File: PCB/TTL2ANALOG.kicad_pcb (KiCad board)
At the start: 2 copper layers, 60.5 x 56.1 mm, 35 parts, among them J1 EGA/CGA, J2 Brown Fix, J3 CSync Inv., J4 Sync Type, J5 TTL Input, J6 Analog Out, J7 Barrel_Jack, U1 GAL16V8, U2 74LS244, U3 74LS244, U4 L78L05

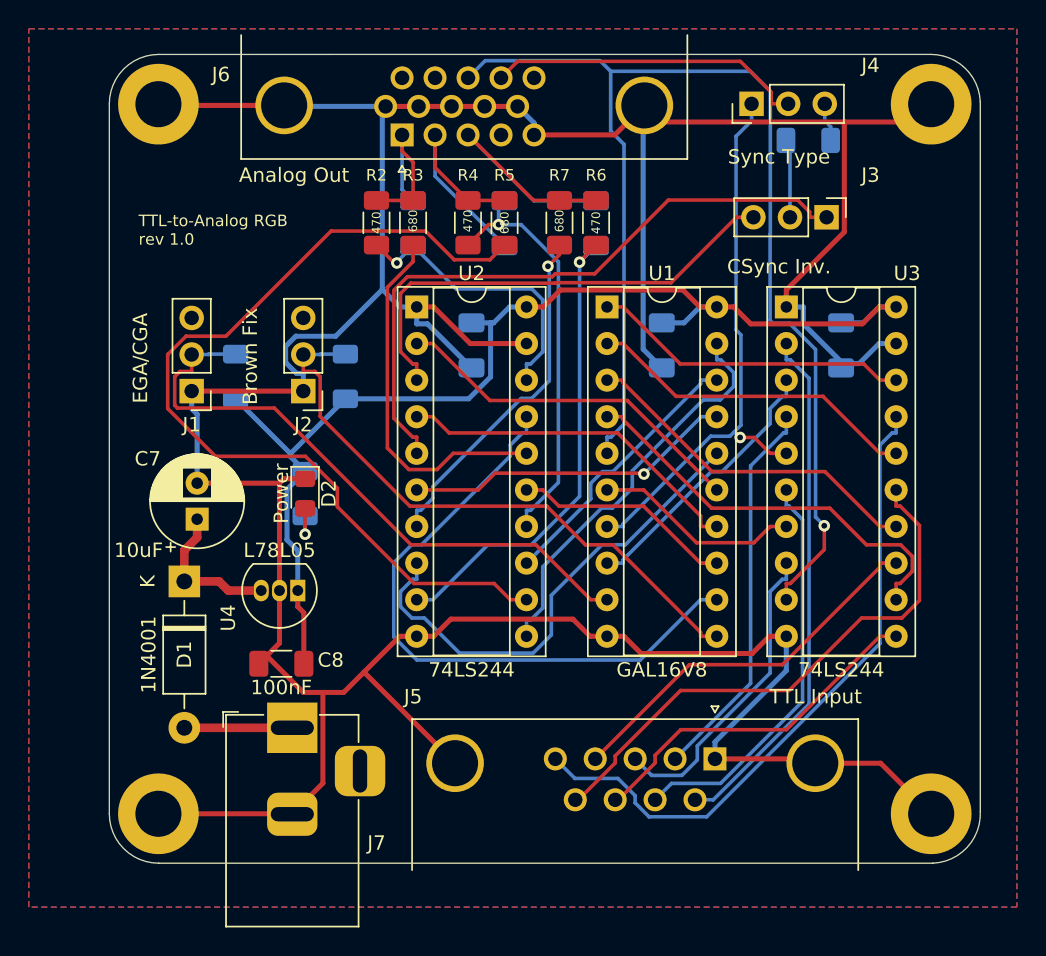
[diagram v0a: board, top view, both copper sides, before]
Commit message: Add pulldown resistor on inputs
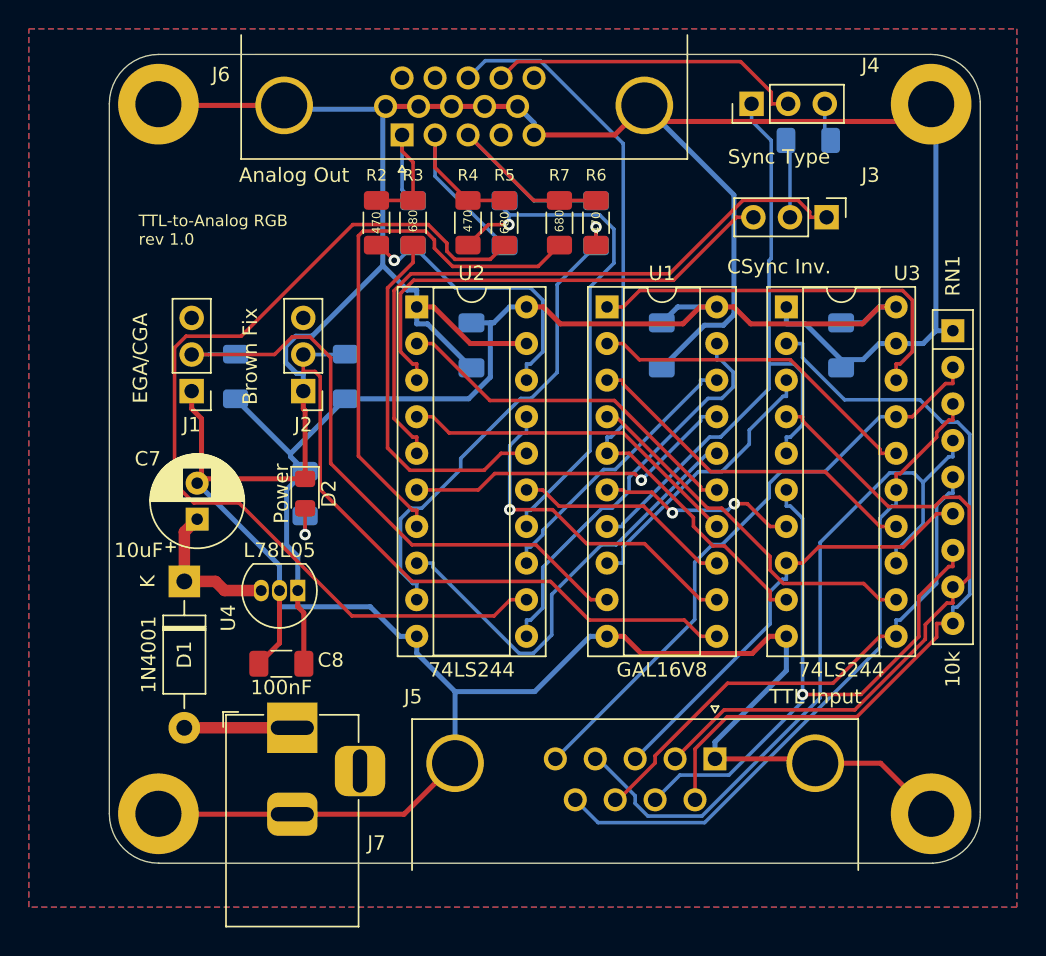
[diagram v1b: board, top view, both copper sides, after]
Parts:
- added RN1: 10k, Resistor_THT:R_Array_SIP9, F.Cu at (165.7, 69.2)
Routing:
- net /IN_HS_BUF: track 88.7 -> 53.1 mm, vias 1 -> 0
- net /IN_G: track 26.7 -> 51.6 mm
- net /IN_R_I: track 27.1 -> 47.9 mm
- net /~DEC_CS: track 44.5 -> 24.1 mm, vias 0 -> 1
- net /IN_G_I: track 36.5 -> 55.3 mm
- net /IN_B_I: track 28.3 -> 45.2 mm, vias 0 -> 1
- net /OUT_B_I: track 24.3 -> 38.1 mm, vias 1 -> 0
- net /IN_HS: track 24.5 -> 37.5 mm
- net GND: track 274.2 -> 286.4 mm
- net /IN_R: track 21.6 -> 31.1 mm
- net /IN_VS: track 38.4 -> 46.3 mm
- net /OUT_G: track 29.2 -> 36.2 mm
- net /IN_G_I_BUF: track 22.2 -> 28.1 mm
- net /IN_VS_BUF: track 39.4 -> 44.5 mm, vias 1 -> 0
- net /IN_B: track 45.8 -> 42.4 mm
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
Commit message: Change PCB, use GAL20V8
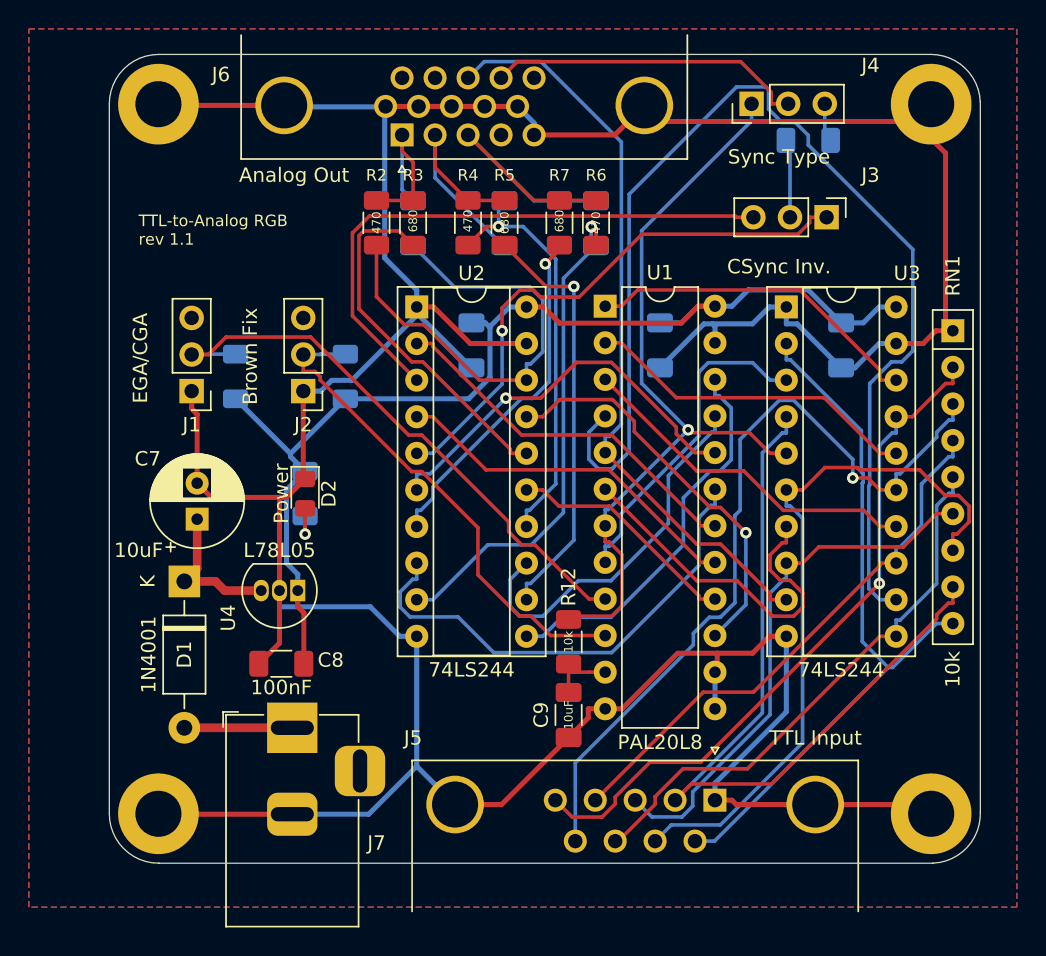
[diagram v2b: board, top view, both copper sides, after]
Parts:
- added C9: 10uF, Capacitor_SMD:C_1206_3216Metric_Pad1.33x1.80mm_HandSolder, F.Cu at (139.1, 95.9)
- added R12: 10k, Resistor_SMD:R_1206_3216Metric_Pad1.30x1.75mm_HandSolder, F.Cu at (139.1, 90.8)
- U1: value GAL16V8 -> PAL20L8; footprint Package_DIP:DIP-20_W7.62mm_Socket -> Package_DIP:DIP-24_W7.62mm
- moved J5 2.87 mm to (149.2, 101.8)
- moved U1 0.14 mm to (141.6, 67.5)
- moved C4 0.13 mm to (145.4, 70.2)
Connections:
- U1 pad 10: GND -> /BRWN_FIX
- U1 pad 11: /BRWN_FIX -> Net-(C9-Pad1)
- U1 pad 12: /~DEC_CS -> GND
- U1 pad 13: /DEC_CS -> GND
- U1 pad 14: /DEC_R_I -> GND
- U1 pad 15: /DEC_R -> /~DEC_CS
- U1 pad 16: /DEC_G_I -> /DEC_CS
- U1 pad 17: /DEC_G -> /DEC_R_I
- U1 pad 18: /DEC_B_I -> /DEC_R
- U1 pad 19: /DEC_B -> /DEC_G_I
- U1 pad 20: VCC -> /DEC_G
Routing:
- net /IN_R_BUF: track 25.9 -> 81.0 mm
- net /OUT_G_I: track 66.3 -> 29.3 mm, vias 0 -> 1
- net /OUT_B_I: track 38.1 -> 24.5 mm, vias 0 -> 1
- net /IN_G: track 51.6 -> 38.3 mm
- net /OUT_R: track 20.1 -> 33.2 mm, vias 1 -> 0
- net /IN_G_BUF: track 14.0 -> 25.2 mm, vias 2 -> 0
- net /BRWN_FIX: track 45.0 -> 34.7 mm
- net /IN_VS: track 46.3 -> 56.3 mm, vias 0 -> 1
- net GND: track 286.4 -> 276.5 mm
- net /IN_VS_BUF: track 44.5 -> 54.1 mm, vias 0 -> 1
- net /IN_R_I: track 47.9 -> 56.2 mm
- net /OUT_G: track 36.2 -> 29.0 mm
- net /~OUT_CS: track 33.3 -> 40.4 mm
- net /DEC_B_I: track 19.5 -> 26.3 mm
- net /OUT_CS: track 45.4 -> 38.9 mm, vias 0 -> 1
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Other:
- board text added: "TTL-to-Analog RGB rev 1.1"
- board text removed: "TTL-to-Analog RGB rev 1.0"

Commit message: Update PCB to add 10k to VCC res to VGA out
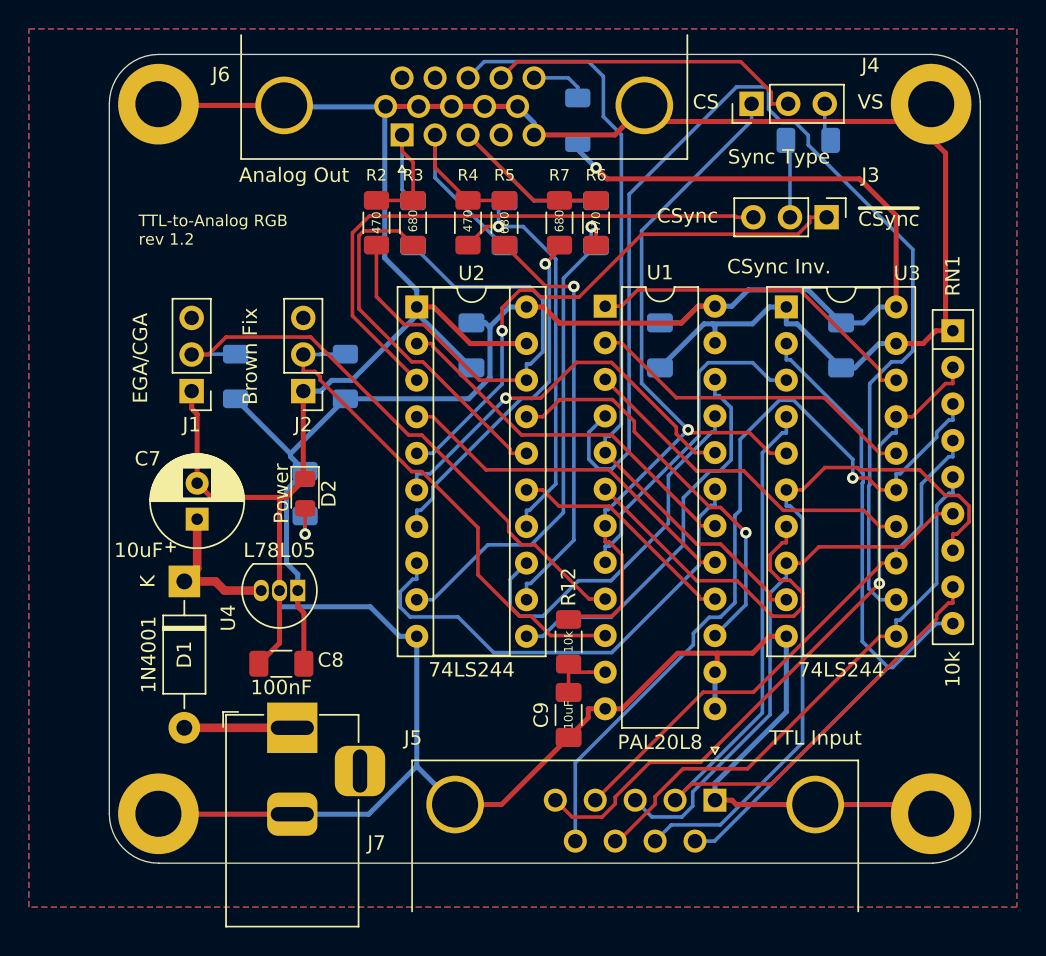
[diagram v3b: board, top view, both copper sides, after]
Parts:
- added R13: 10k, Resistor_SMD:R_1206_3216Metric_Pad1.30x1.75mm_HandSolder, B.Cu at (139.7, 54.6)
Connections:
- J6 pad 15: (no net) -> Net-(J6-Pad15)
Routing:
- net VCC: track 78.3 -> 109.1 mm, vias 0 -> 1
- net Net-(J6-Pad15): track 0.00 -> 4.04 mm
- net /IN_HS_BUF: track 52.7 -> 54.6 mm
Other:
- board text added: "CS"
- board text added: "CSync"
- board text added: "TTL-to-Analog RGB rev 1.2"
- board text added: "VS"
- board text added: "~CSync"
- board text removed: "TTL-to-Analog RGB rev 1.1"
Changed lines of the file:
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@@
-(kicad_pcb (version 20171130) (host pcbnew 5.1.10-1.fc34)
+(kicad_pcb (version 20171130) (host pcbnew 5.1.10-6.fc34)
   (general
     (thickness 1.6)
-    (drawings 10)
-    (tracks 579)
+    (drawings 14)
+    (tracks 591)
     (zones 0)
-    (modules 38)
-    (nets 47)
+    (modules 39)
+    (nets 48)
   )
   (page A4)
@@
     (31 B.Cu signal)
     (32 B.Adhes user)
-    (33 F.Adhes user)
+    (33 F.Adhes user hide)
     (34 B.Paste user)
     (35 F.Paste user)
@@
   (net 45 /IN_G_I_BUF)
   (net 46 "Net-(C9-Pad1)")
+  (net 47 "Net-(J6-Pad15)")
   (net_class Default "This is the default net class."
     (clearance 0.2)
@@
     (add_net GND)
     (add_net VCC)
+  )
+  (module Resistor_SMD:R_1206_3216Metric_Pad1.30x1.75mm_HandSolder (layer B.Cu)
+    (at 139.7 54.61 270)
+    (descr "Resistor SMD 1206 (3216 Metric), square (rectangular) end terminal, IPC_7351 nominal with elongated pad for handsoldering. (Body size source: IPC-SM-782 page 72, https://www.pcb-3d.com/wordpress/wp-content/uploads/ipc-sm-782a_amendment_1_and_2.pdf), generated with kicad-footprint-generator")
+    (tags "resistor handsolder")
+    (attr smd)
+    (fp_text reference R13 (at -3.048 0 180) (layer B.SilkS)
+      (effects (font (size 1 1) (thickness 0.15)) (justify mirror))
+    )
+    (fp_text value 10k (at 0 0 90) (layer B.SilkS)
+      (effects (font (size 0.6 0.6) (thickness 0.15)) (justify mirror))
+    )
+    (fp_text user %R (at 0 0 90) (layer B.Fab)
+      (effects (font (size 0.8 0.8) (thickness 0.12)) (justify mirror))
+    )
+    (fp_line (start -1.6 -0.8) (end -1.6 0.8) (layer B.Fab) (width 0.1))
+    (fp_line (start -1.6 0.8) (end 1.6 0.8) (layer B.Fab) (width 0.1))
+    (fp_line (start 1.6 0.8) (end 1.6 -0.8) (layer B.Fab) (width 0.1))
+    (fp_line (start 1.6 -0.8) (end -1.6 -0.8) (layer B.Fab) (width 0.1))
+    (fp_line (start -0.727064 0.91) (end 0.727064 0.91) (layer B.SilkS) (width 0.12))
+    (fp_line (start -0.727064 -0.91) (end 0.727064 -0.91) (layer B.SilkS) (width 0.12))
+    (fp_line (start -2.45 -1.12) (end -2.45 1.12) (layer B.CrtYd) (width 0.05))
+    (fp_line (start -2.45 1.12) (end 2.45 1.12) (layer B.CrtYd) (width 0.05))
+    (fp_line (start 2.45 1.12) (end 2.45 -1.12) (layer B.CrtYd) (width 0.05))
+    (fp_line (start 2.45 -1.12) (end -2.45 -1.12) (layer B.CrtYd) (width 0.05))
+    (pad 2 smd roundrect (at 1.55 0 270) (size 1.3 1.75) (layers B.Cu B.Paste B.Mask) (roundrect_rratio 0.192308)
+      (net 2 VCC))
+    (pad 1 smd roundrect (at -1.55 0 270) (size 1.3 1.75) (layers B.Cu B.Paste B.Mask) (roundrect_rratio 0.192308)
+      (net 47 "Net-(J6-Pad15)"))
+    (model ${KISYS3DMOD}/Resistor_SMD.3dshapes/R_1206_3216Metric.wrl
+      (at (xyz 0 0 0))
+      (scale (xyz 1 1 1))
+      (rotate (xyz 0 0 0))
+    )
   )
   (module Package_DIP:DIP-24_W7.62mm (layer F.Cu)
@@
     (pad 0 thru_hole circle (at -16.815 2.05 180) (size 4 4) (drill 3.2) (layers *.Cu *.Mask)
       (net 1 GND))
-    (pad 15 thru_hole circle (at -9.16 3.96 180) (size 1.6 1.6) (drill 1) (layers *.Cu *.Mask))
+    (pad 15 thru_hole circle (at -9.16 3.96 180) (size 1.6 1.6) (drill 1) (layers *.Cu *.Mask)
+      (net 47 "Net-(J6-Pad15)"))
     (pad 14 thru_hole circle (at -6.87 3.96 180) (size 1.6 1.6) (drill 1) (layers *.Cu *.Mask)
       (net 37 /SYNC_OUT))
@@
     )
   )
-  (gr_text "TTL-to-Analog RGB\nrev 1.1" (at 109.22 62.23) (layer F.SilkS)
+  (gr_text VS (at 160.02 53.34) (layer F.SilkS)
+    (effects (font (size 1 1) (thickness 0.25)))
+  )
+  (gr_text CS (at 148.59 53.34) (layer F.SilkS)
+    (effects (font (size 1 1) (thickness 0.25)))
+  )
+  (gr_text ~CSync (at 161.29 61.471) (layer F.SilkS)
+    (effects (font (size 1 1) (thickness 0.25)))
+  )
+  (gr_text CSync (at 147.32 61.2485) (layer F.SilkS)
+    (effects (font (size 1 1) (thickness 0.25)))
+  )
+  (gr_text "TTL-to-Analog RGB\nrev 1.2" (at 109.22 62.23) (layer F.SilkS)
     (effects (font (size 0.8 0.8) (thickness 0.15)) (justify left))
   )
@@
   (segment (start 145.405 68.6685) (end 146.8952 68.6685) (width 0.35) (layer B.Cu) (net 2))
   (segment (start 146.8952 68.6685) (end 148.0497 67.514) (width 0.35) (layer B.Cu) (net 2))
+  (via (at 140.97 57.912) (size 0.8) (drill 0.4) (layers F.Cu B.Cu) (net 2))
+  (segment (start 139.7 56.642) (end 140.97 57.912) (width 0.35) (layer B.Cu) (net 2))
+  (segment (start 139.7 56.16) (end 139.7 56.642) (width 0.35) (layer B.Cu) (net 2))
+  (segment (start 140.97 57.912) (end 141.732 58.674) (width 0.35) (layer F.Cu) (net 2))
+  (segment (start 141.732 58.674) (end 159.258 58.674) (width 0.35) (layer F.Cu) (net 2))
+  (segment (start 161.798 61.214) (end 161.798 67.564) (width 0.35) (layer F.Cu) (net 2))
+  (segment (start 159.258 58.674) (end 161.798 61.214) (width 0.35) (layer F.Cu) (net 2))
   (segment (start 165.735 74.295) (end 165.735 75.4203) (width 0.25) (layer B.Cu) (net 3))
   (segment (start 161.798 80.264) (end 161.798 79.1387) (width 0.25) (layer B.Cu) (net 3))
@@
   (segment (start 149.6147 84.024) (end 153.0527 87.462) (width 0.25) (layer F.Cu) (net 39))
   (segment (start 153.0527 87.462) (end 153.0527 87.884) (width 0.25) (layer F.Cu) (net 39))
+  (segment (start 133.2158 50.5382) (end 132.088 51.666) (width 0.25) (layer B.Cu) (net 39))
+  (segment (start 140.4542 50.5382) (end 133.2158 50.5382) (width 0.25) (layer B.Cu) (net 39))
+  (segment (start 141.478 51.562) (end 140.4542 50.5382) (width 0.25) (layer B.Cu) (net 39))
+  (segment (start 142.7303 75.7048) (end 142.7303 55.6083) (width 0.25) (layer B.Cu) (net 39))
+  (segment (start 141.605 76.5487) (end 141.8864 76.5487) (width 0.25) (layer B.Cu) (net 39))
+  (segment (start 141.478 54.356) (end 141.478 51.562) (width 0.25) (layer B.Cu) (net 39))
+  (segment (start 142.7303 55.6083) (end 141.478 54.356) (width 0.25) (layer B.Cu) (net 39))
+  (segment (start 141.8864 76.5487) (end 142.7303 75.7048) (width 0.25) (layer B.Cu) (net 39))
   (segment (start 141.605 77.674) (end 141.605 76.5487) (width 0.25) (layer B.Cu) (net 39))
-  (segment (start 132.088 51.666) (end 133.2158 50.5382) (width 0.25) (layer B.Cu) (net 39))
-  (segment (start 133.2158 50.5382) (end 137.1497 50.5382) (width 0.25) (layer B.Cu) (net 39))
-  (segment (start 137.1497 50.5382) (end 142.7303 56.1188) (width 0.25) (layer B.Cu) (net 39))
-  (segment (start 142.7303 56.1188) (end 142.7303 75.7048) (width 0.25) (layer B.Cu) (net 39))
-  (segment (start 142.7303 75.7048) (end 141.8864 76.5487) (width 0.25) (layer B.Cu) (net 39))
-  (segment (start 141.8864 76.5487) (end 141.605 76.5487) (width 0.25) (layer B.Cu) (net 39))
   (segment (start 141.605 84.1687) (end 141.8864 84.1687) (width 0.25) (layer B.Cu) (net 40))
   (segment (start 141.8864 84.1687) (end 142.7303 83.3248) (width 0.25) (layer B.Cu) (net 40))
@@
   (segment (start 139.065 92.914) (end 140.4797 92.914) (width 0.25) (layer F.Cu) (net 46))
   (segment (start 141.605 92.914) (end 140.4797 92.914) (width 0.25) (layer F.Cu) (net 46))
+  (segment (start 136.668 51.666) (end 139.042 51.666) (width 0.25) (layer B.Cu) (net 47))
+  (segment (start 139.7 52.324) (end 139.7 53.06) (width 0.25) (layer B.Cu) (net 47))
+  (segment (start 139.042 51.666) (end 139.7 52.324) (width 0.25) (layer B.Cu) (net 47))
   (zone (net 1) (net_name GND) (layer F.Cu) (hatch edge 0.508)
     (connect_pads (clearance 0.508))
